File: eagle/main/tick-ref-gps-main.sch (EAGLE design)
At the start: 51 parts, among them CN1 1PPS Out, CN2 ISP, CN3 RS232, CN4 Power In, CN5 Serial Program, U1 ATMEGA168-AU, U2 AS1115, U3 MAX232, U4 LM2931_FIXED, X1 16MHz

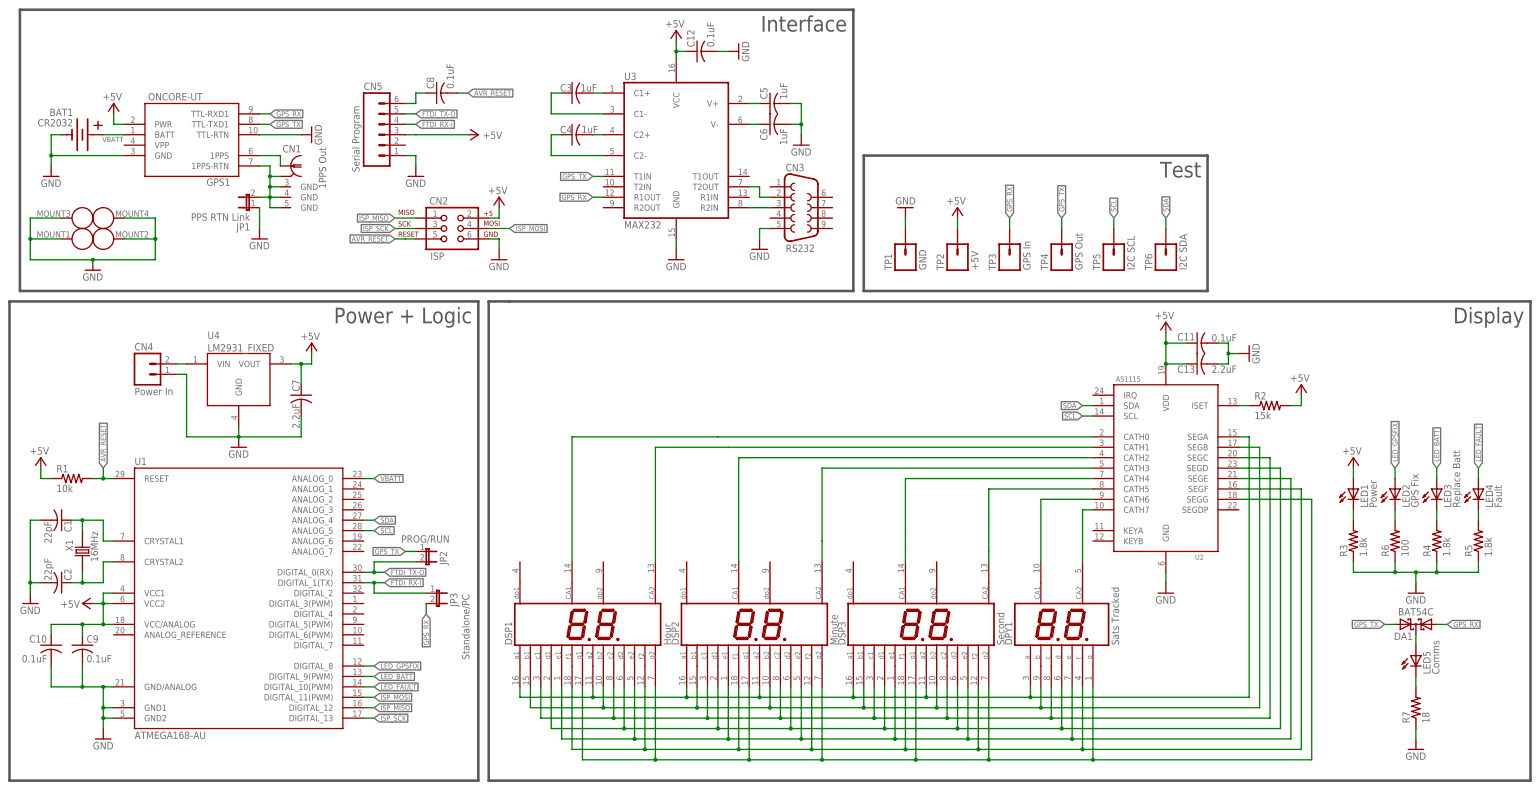
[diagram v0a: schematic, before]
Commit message: New main board design schematic done, half-routed.
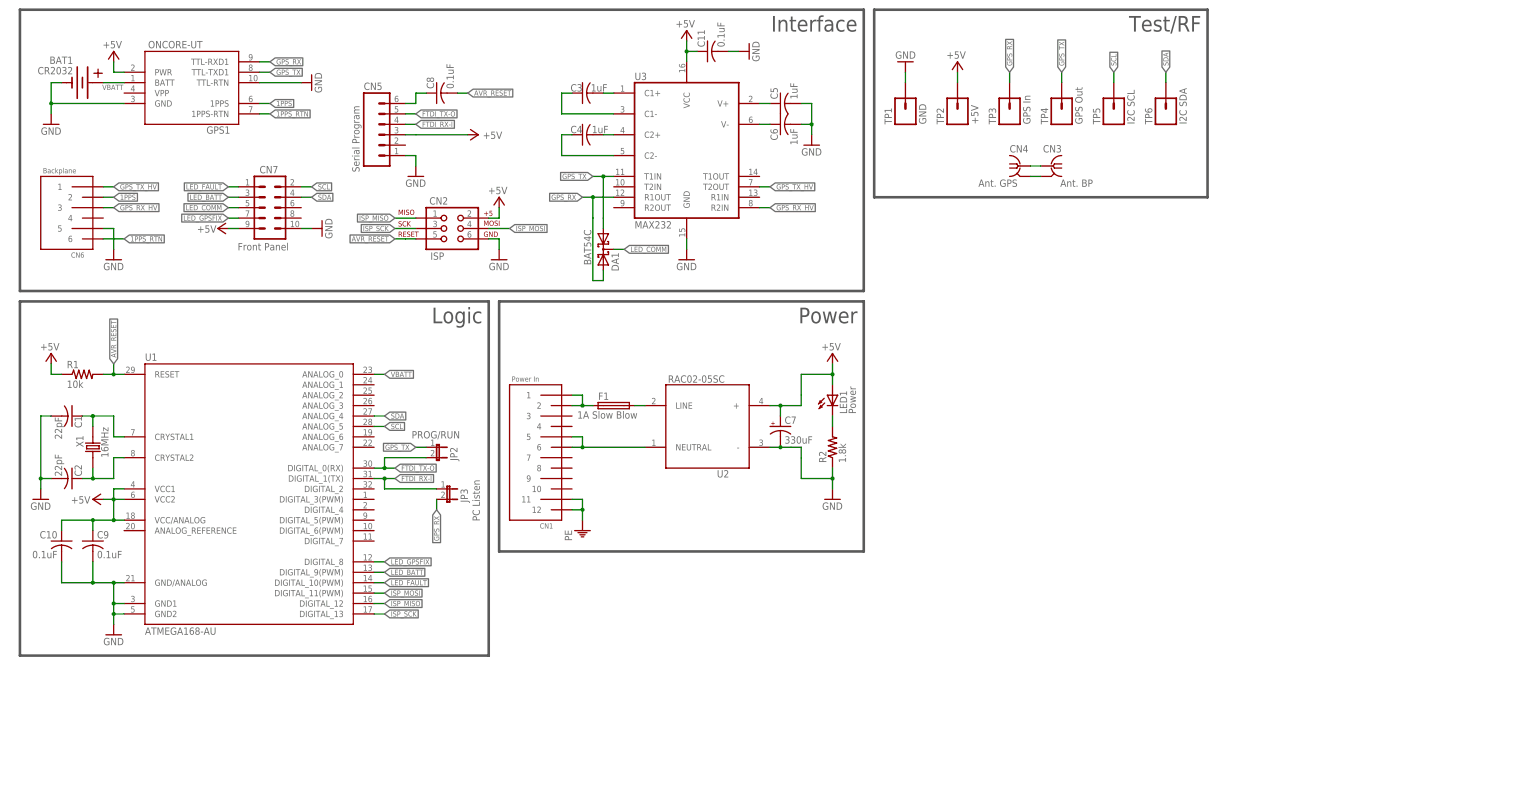
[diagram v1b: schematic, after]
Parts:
- removed C12: 0.1uF, rcl:C-USC0603
- removed C13: 2.2uF, rcl:C-USC0805
- removed DPY1: Sats Tracked, led-sen:LUMEX-LDD-F302NI
- removed DSP1: Hour, display-hp:HD-K121
- removed DSP2: Minute, display-hp:HD-K121
- removed DSP3: Second, display-hp:HD-K121
- removed JP1: PPS RTN Link, SparkFun:JUMPER-2SMD-NO
- removed LED2: GPS Fix, led:LED5MM
- removed LED3: Replace Batt, led:LED5MM
- removed LED4: Fault, led:LED5MM
- removed LED5: Comms, led:LED5MM
- removed R3, R4, R5: 1.8k, rcl:R-US_R0603
- removed R6: 100, rcl:R-US_R0603
- removed R7: 18, rcl:R-US_R0603
- removed U4: LM2931_FIXED, SparkFun-PowerIC:LM2931_FIXED
- added CN6: Backplane, con-sen:EDGECON-M-0.1-6
- added CN7: Front Panel, SparkFun-Connectors:M05X2PTH
- added F1: 1A Slow Blow, fuse:SH22,5A
- C7: value 2.2uF -> 330uF; device rcl:C-USC0805 -> rcl:CPOL-USE5-10.5
- CN1: value 1PPS Out -> Power In; device con-coax:B35N57 -> con-sen:EDGECON-M-0.15-12
- CN3: value RS232 -> Ant. BP; device con-subd:F09VP -> con-samtec:COAX
- CN4: value Power In -> Ant. GPS; device SparkFun:M02POLAR_LOCK -> con-sen:MOLEX-MCX-V
- JP3: value Standalone/PC -> PC Listen
- LED1: device led:LED5MM -> led:LEDCHIP-LED0603
- R2: value 15k -> 1.8k
- U2: value AS1115 -> RAC02-05SC; device austria-sen:AS1115 -> recom-sen:RAC0X-SC
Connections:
- removed net CATH_HOUR_LS: DSP1.CA2, U2.CATH1
- removed net CATH_HOUR_MS: DSP1.CA1, U2.CATH0
- removed net CATH_MIN_LS: DSP2.CA2, U2.CATH3
- removed net CATH_MIN_MS: DSP2.CA1, U2.CATH2
- removed net CATH_SATS_LS: DPY1.CA2, U2.CATH7
- removed net CATH_SATS_MS: DPY1.CA1, U2.CATH6
- removed net CATH_SEC_LS: DSP3.CA2, U2.CATH5
- removed net CATH_SEC_MS: DSP3.CA1, U2.CATH4
- removed net LED1_R: LED1.C, R3.2
- removed net LED2_R: LED2.C, R6.2
- removed net LED3_R: LED3.C, R4.2
- removed net LED4_R: LED4.C, R5.2
- removed net LED5_D: DA1.CC, LED5.A
- removed net LED5_R: LED5.C, R7.2
- removed net LED_ISET: R2.1, U2.ISET
- removed net LED_SEG_A: DPY1.A, DSP1.A1, DSP1.A2, DSP2.A1, DSP2.A2, DSP3.A1, DSP3.A2, U2.SEGA
- removed net LED_SEG_B: DPY1.B, DSP1.B1, DSP1.B2, DSP2.B1, DSP2.B2, DSP3.B1, DSP3.B2, U2.SEGB
- removed net LED_SEG_C: DPY1.C, DSP1.C1, DSP1.C2, DSP2.C1, DSP2.C2, DSP3.C1, DSP3.C2, U2.SEGC
- removed net LED_SEG_D: DPY1.D, DSP1.D1, DSP1.D2, DSP2.D1, DSP2.D2, DSP3.D1, DSP3.D2, U2.SEGD
- removed net LED_SEG_E: DPY1.E, DSP1.E1, DSP1.E2, DSP2.E1, DSP2.E2, DSP3.E1, DSP3.E2, U2.SEGE
- removed net LED_SEG_F: DPY1.F, DSP1.F1, DSP1.F2, DSP2.F1, DSP2.F2, DSP3.F1, DSP3.F2, U2.SEGF
- removed net LED_SEG_G: DPY1.G, DSP1.G1, DSP1.G2, DSP2.G1, DSP2.G2, DSP3.G1, DSP3.G2, U2.SEGG
- removed net VIN: CN4.2, U4.VIN
- new net ANTENNA-GND: CN3COAX.GND, CN4.GND
- new net ANTENNA-RF: CN3COAX.1, CN4.A
- new net LED_COMM: CN7.5, DA1.CC
- new net LINE: F1.2, U2.LINE
- new net LINE-PREFUSE: CN1.1, CN1.2, F1.1
- new net N$1: LED1.C, R2.2
- new net NEUTRAL: CN1.5, CN1.6, U2.NEUTRAL
- new net PE: CN1.11, CN1.12
- net +5V: now also C7.+, CN7.9, U2.+; no longer C12.1, C13.1, C7.1, R2.2, U2.VDD, U4.VOUT
- net 1PPS: now also CN6.2; no longer CN1G$1.1
- net 1PPS_RTN: now also CN6.6; no longer CN1G$1.GND, CN1G2.GND, CN1G3.GND, CN1G4.GND, JP1.2
- net GND: now also C7.-, CN6.5, CN7.10, R2.1, U2.-; no longer C12.2, C13.2, C7.2, CN3.5, CN4.1, GPS1G$2.MOUNTHOLE1, GPS1G$2.MOUNTHOLE2, GPS1G$2.MOUNTHOLE3, GPS1G$2.MOUNTHOLE4, JP1.1, R3.1, R4.1, R5.1, R6.1, R7.1, U2.GND, U4.GND
- net GPS_RX: now also DA1.A2; no longer DA1.A1
- net GPS_RX_HV: now also CN6.3; no longer CN3.3
- net GPS_TX: now also DA1.A1; no longer DA1.A2
- net GPS_TX_HV: now also CN6.1; no longer CN3.2
- net LED_BATT: now also CN7.3; no longer LED3.A
- net LED_FAULT: now also CN7.1; no longer LED4.A
- net LED_GPSFIX: now also CN7.7; no longer LED2.A
- net SCL: now also CN7.2; no longer U2.SCL
- net SDA: now also CN7.4; no longer U2.SDA
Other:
- note added: "Logic"
- note added: "Power"
- note added: "Test/RF"
- note removed: "Display"
- note removed: "Power + Logic"
- note removed: "Test"
- moved on the sheet: BAT1, C1, C10, C11, C2, C3, C4, C5, C6, C9, CN4, DA1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

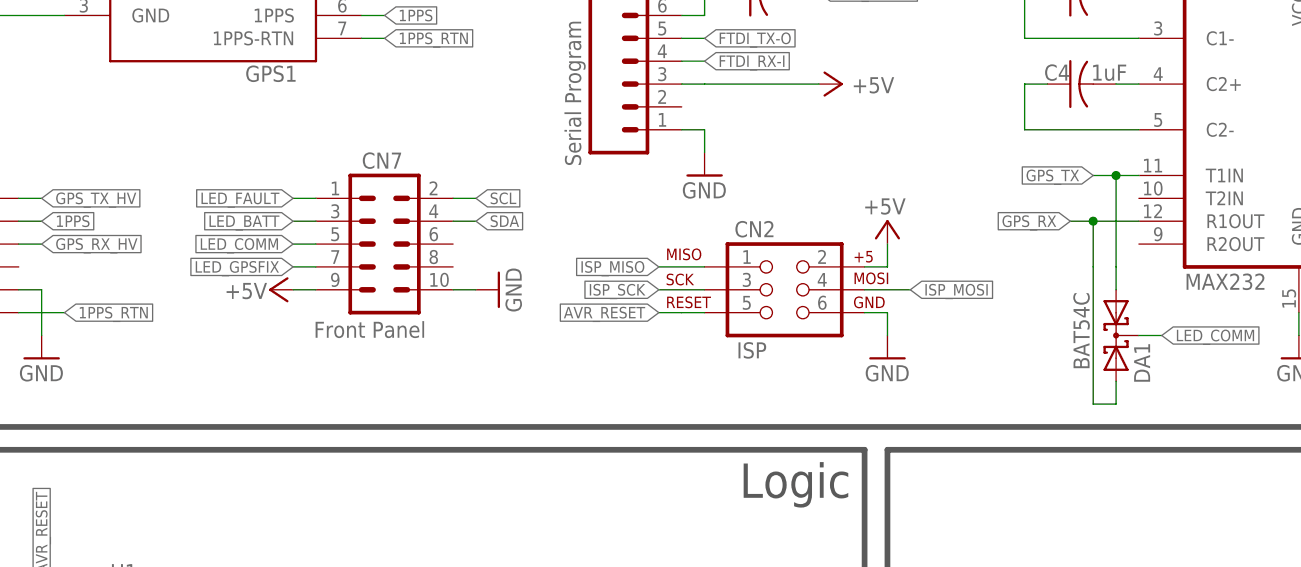
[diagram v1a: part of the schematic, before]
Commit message: Finished routing board, need to run through checklist tomorrow before CAMing.
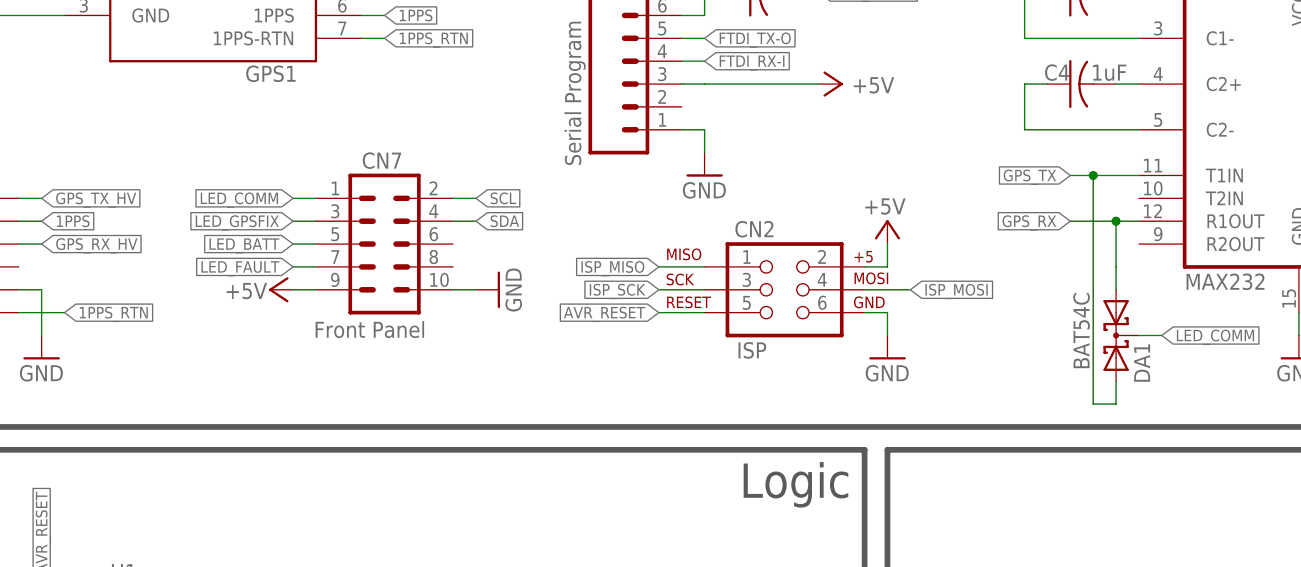
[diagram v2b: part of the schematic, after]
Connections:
- net N$1 renamed LED1_R
- net GPS_RX: now also DA1.A1; no longer DA1.A2
- net GPS_TX: now also DA1.A2; no longer DA1.A1
- net LED_BATT: now also CN7.5; no longer CN7.3
- net LED_COMM: now also CN7.1; no longer CN7.5
- net LED_FAULT: now also CN7.7; no longer CN7.1
- net LED_GPSFIX: now also CN7.3; no longer CN7.7
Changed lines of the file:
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@@
 <class number="0" name="default" width="0" drill="0">
+</class>
+<class number="1" name="PE" width="1.016" drill="0">
+<clearance class="1" value="0.508"/>
 </class>
 </classes>
@@
 </segment>
 <segment>
-<pinref part="CN7" gate="G$1" pin="7"/>
-<wire x1="53.34" y1="137.16" x2="50.8" y2="137.16" width="0.1524" layer="91"/>
-<label x="50.8" y="137.16" size="1.27" layer="95" rot="R180" xref="yes"/>
+<pinref part="CN7" gate="G$1" pin="3"/>
+<wire x1="53.34" y1="142.24" x2="50.8" y2="142.24" width="0.1524" layer="91"/>
+<label x="50.8" y="142.24" size="1.27" layer="95" rot="R180" xref="yes"/>
 </segment>
 </net>
@@
 </segment>
 <segment>
-<pinref part="CN7" gate="G$1" pin="3"/>
-<wire x1="53.34" y1="142.24" x2="50.8" y2="142.24" width="0.1524" layer="91"/>
-<label x="50.8" y="142.24" size="1.27" layer="95" rot="R180" xref="yes"/>
+<pinref part="CN7" gate="G$1" pin="5"/>
+<wire x1="53.34" y1="139.7" x2="50.8" y2="139.7" width="0.1524" layer="91"/>
+<label x="50.8" y="139.7" size="1.27" layer="95" rot="R180" xref="yes"/>
 </segment>
 </net>
@@
 <segment>
 <pinref part="U3" gate="G$1" pin="T1IN"/>
-<wire x1="144.78" y1="147.32" x2="142.24" y2="147.32" width="0.1524" layer="91"/>
-<label x="139.7" y="147.32" size="1.27" layer="95" rot="R180" xref="yes"/>
-<wire x1="142.24" y1="147.32" x2="139.7" y2="147.32" width="0.1524" layer="91"/>
-<wire x1="142.24" y1="147.32" x2="142.24" y2="137.16" width="0.1524" layer="91"/>
-<junction x="142.24" y="147.32"/>
-<pinref part="DA1" gate="G$1" pin="A1"/>
-<wire x1="142.24" y1="134.62" x2="142.24" y2="137.16" width="0.1524" layer="91"/>
+<wire x1="144.78" y1="147.32" x2="139.7" y2="147.32" width="0.1524" layer="91"/>
+<label x="137.16" y="147.32" size="1.27" layer="95" rot="R180" xref="yes"/>
+<wire x1="139.7" y1="147.32" x2="137.16" y2="147.32" width="0.1524" layer="91"/>
+<wire x1="139.7" y1="147.32" x2="139.7" y2="121.92" width="0.1524" layer="91"/>
+<junction x="139.7" y="147.32"/>
+<pinref part="DA1" gate="G$1" pin="A2"/>
+<wire x1="142.24" y1="124.46" x2="142.24" y2="121.92" width="0.1524" layer="91"/>
+<wire x1="142.24" y1="121.92" x2="139.7" y2="121.92" width="0.1524" layer="91"/>
 </segment>
 <segment>
@@
 <segment>
 <pinref part="U3" gate="G$1" pin="R1OUT"/>
-<wire x1="144.78" y1="142.24" x2="139.7" y2="142.24" width="0.1524" layer="91"/>
+<wire x1="144.78" y1="142.24" x2="142.24" y2="142.24" width="0.1524" layer="91"/>
 <label x="137.16" y="142.24" size="1.27" layer="95" rot="R180" xref="yes"/>
-<wire x1="139.7" y1="142.24" x2="137.16" y2="142.24" width="0.1524" layer="91"/>
-<wire x1="139.7" y1="142.24" x2="139.7" y2="137.16" width="0.1524" layer="91"/>
-<junction x="139.7" y="142.24"/>
-<wire x1="139.7" y1="137.16" x2="139.7" y2="121.92" width="0.1524" layer="91"/>
-<pinref part="DA1" gate="G$1" pin="A2"/>
-<wire x1="139.7" y1="121.92" x2="142.24" y2="121.92" width="0.1524" layer="91"/>
-<wire x1="142.24" y1="121.92" x2="142.24" y2="124.46" width="0.1524" layer="91"/>
+<wire x1="142.24" y1="142.24" x2="137.16" y2="142.24" width="0.1524" layer="91"/>
+<wire x1="142.24" y1="142.24" x2="142.24" y2="137.16" width="0.1524" layer="91"/>
+<junction x="142.24" y="142.24"/>
+<pinref part="DA1" gate="G$1" pin="A1"/>
+<wire x1="142.24" y1="137.16" x2="142.24" y2="134.62" width="0.1524" layer="91"/>
 </segment>
 <segment>
@@
 </segment>
 <segment>
-<pinref part="CN7" gate="G$1" pin="1"/>
-<wire x1="53.34" y1="144.78" x2="50.8" y2="144.78" width="0.1524" layer="91"/>
-<label x="50.8" y="144.78" size="1.27" layer="95" rot="R180" xref="yes"/>
+<pinref part="CN7" gate="G$1" pin="7"/>
+<wire x1="53.34" y1="137.16" x2="50.8" y2="137.16" width="0.1524" layer="91"/>
+<label x="50.8" y="137.16" size="1.27" layer="95" rot="R180" xref="yes"/>
 </segment>
 </net>
@@
 </segment>
 <segment>
-<pinref part="CN7" gate="G$1" pin="5"/>
-<wire x1="50.8" y1="139.7" x2="53.34" y2="139.7" width="0.1524" layer="91"/>
-<label x="50.8" y="139.7" size="1.27" layer="95" rot="R180" xref="yes"/>
+<pinref part="CN7" gate="G$1" pin="1"/>
+<wire x1="50.8" y1="144.78" x2="53.34" y2="144.78" width="0.1524" layer="91"/>
+<label x="50.8" y="144.78" size="1.27" layer="95" rot="R180" xref="yes"/>
 </segment>
 </net>
@@
 </segment>
 </net>
-<net name="PE" class="0">
+<net name="PE" class="1">
 <segment>
 <pinref part="CN1" gate="G$1" pin="11"/>
@@
 </segment>
 </net>
-<net name="N$1" class="0">
+<net name="LED1_R" class="0">
 <segment>
 <pinref part="R2" gate="G$1" pin="2"/>
